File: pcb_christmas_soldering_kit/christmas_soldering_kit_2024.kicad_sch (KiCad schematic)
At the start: 23 parts, among them J3 Conn_Out, J4 Conn_In, J5 J_In, P1 Conn_01x08_Pin, P2 Conn_01x08_Pin, SW1 Button, U1 ESP32-C3, U2 TC4427CPA

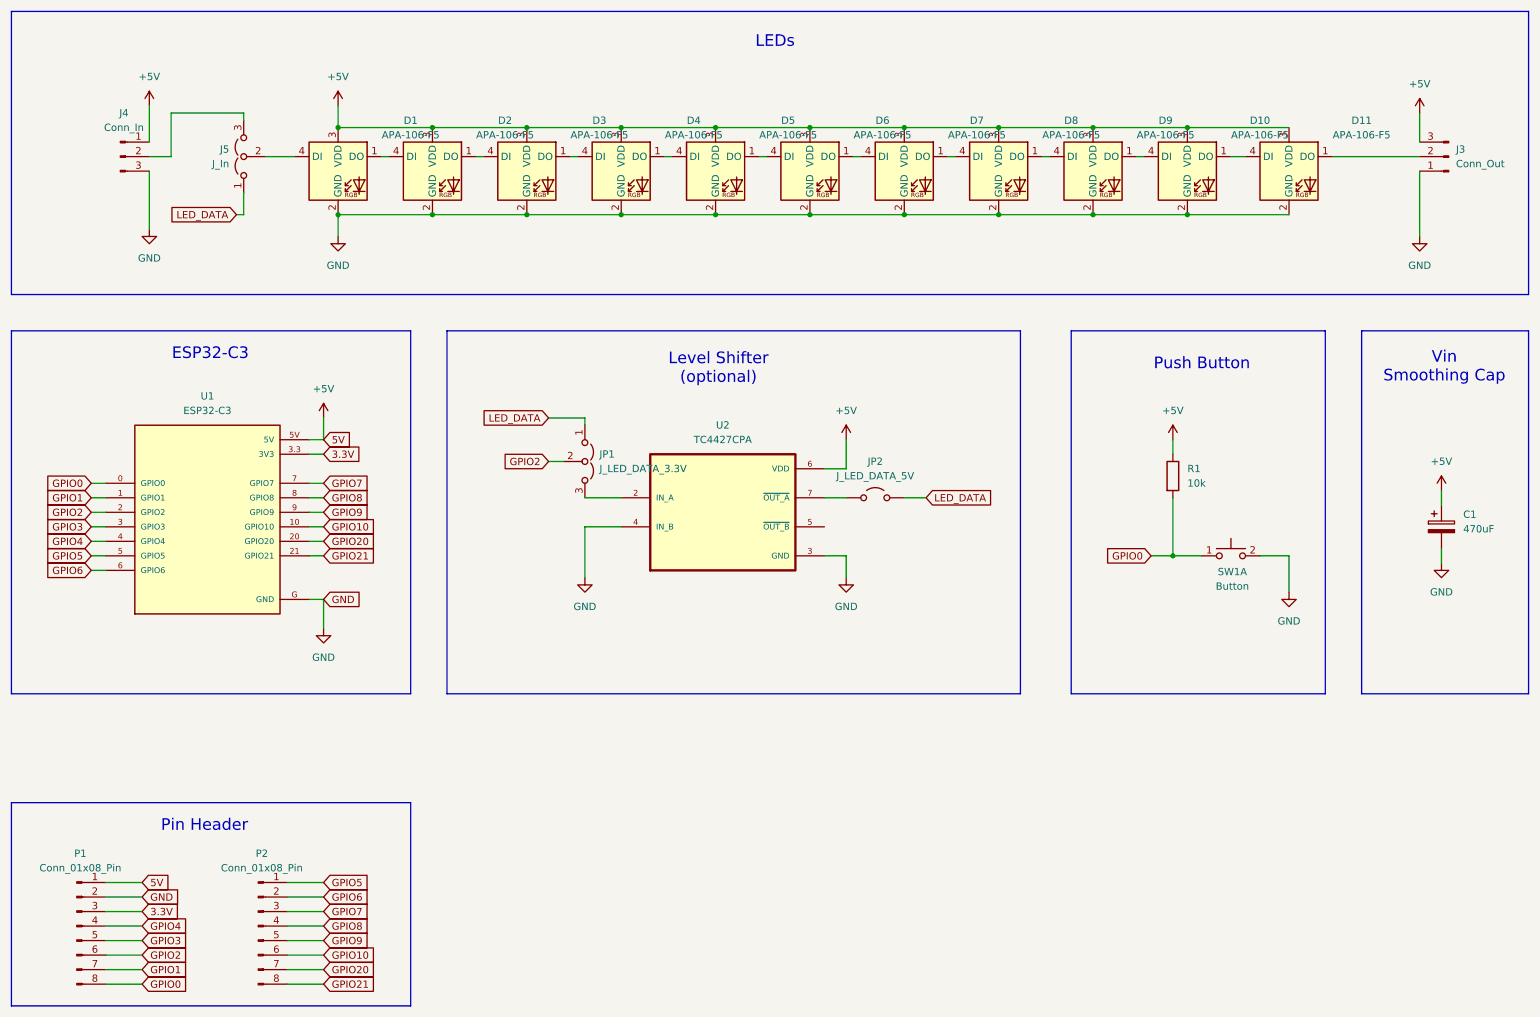
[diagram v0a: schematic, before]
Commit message: prototype 2: remove unnecessary components, improve LED footprints
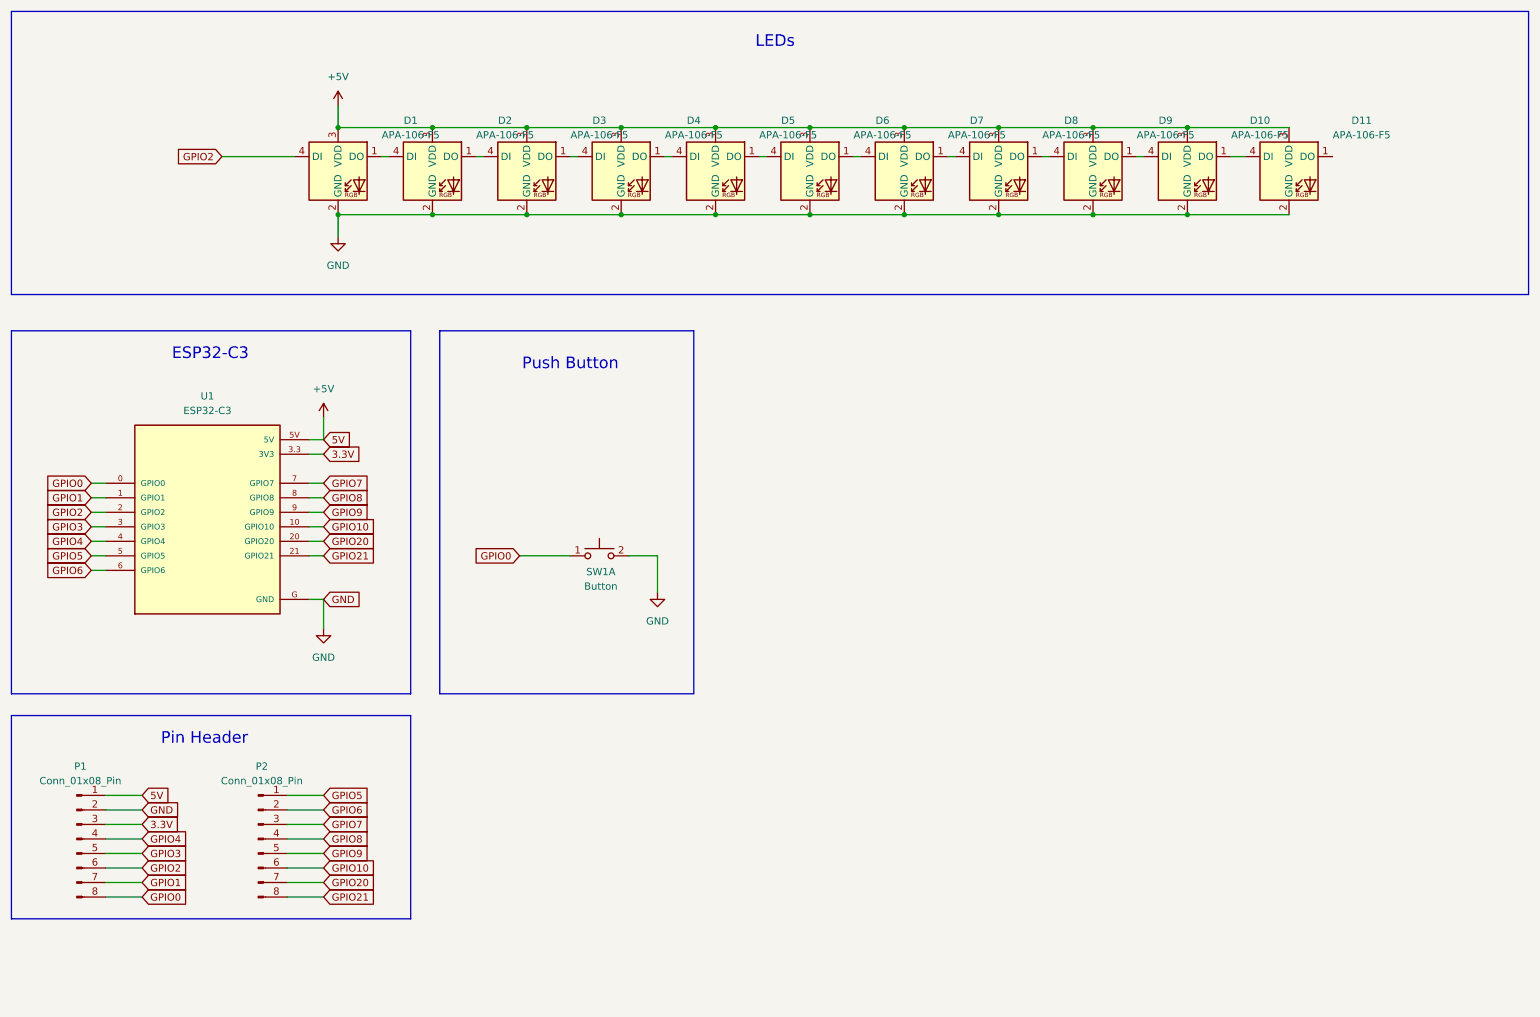
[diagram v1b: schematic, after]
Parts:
- removed C1: 470uF, Capacitor_THT:CP_Radial_D5.0mm_P2.50mm, symbol Device:C_Polarized
- removed J3: Conn_Out, Connector_JST:JST_XH_S3B-XH-A_1x03_P2.50mm_Horizontal, symbol Connector:Conn_01x03_Pin
- removed J4: Conn_In, Connector_JST:JST_XH_S3B-XH-A_1x03_P2.50mm_Horizontal, symbol Connector:Conn_01x03_Pin
- removed J5: J_In, Connector_PinHeader_2.54mm:PinHeader_1x03_P2.54mm_Vertical, symbol Jumper:Jumper_3_Open
- removed JP1: J_LED_DATA_3.3V, Jumper:SolderJumper-3_P1.3mm_Open_Pad1.0x1.5mm_NumberLabels, symbol Jumper:Jumper_3_Open
- removed JP2: J_LED_DATA_5V, Jumper:SolderJumper-2_P1.3mm_Open_TrianglePad1.0x1.5mm, symbol Jumper:Jumper_2_Open
- removed R1: 10k, Resistor_THT:R_Axial_DIN0207_L6.3mm_D2.5mm_P10.16mm_Horizontal, symbol Device:R
- removed U2: TC4427CPA, Package_DIP:DIP-8_W7.62mm, symbol TC4427CPA:TC4427CPA
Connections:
- net GPIO2: now also D1.4 (DI)
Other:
- note removed: "Level Shifter (optional)"
- note removed: "Vin Smoothing Cap"
- moved on the sheet: P1, P2, SW1A

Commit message: final version, rev. 1.0: ordered
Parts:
- added H1: MountingHole, MountingHole:MountingHole_2.2mm_M2, symbol Mechanical:MountingHole
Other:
- note added: "Mounting Hole"
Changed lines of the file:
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@@
+	)
+	(rectangle
+		(start 90.17 143.51)
+		(end 134.62 179.07)
+		(stroke
+			(width 0)
+			(type default)
+		)
+		(fill
+			(type none)
+		)
 	)
 	(rectangle
@@
 		)
 	)
+	(text "Mounting Hole"
+		(exclude_from_sim no)
+		(at 111.506 147.574 0)
+		(effects
+			(font
+				(size 2.032 2.032)
+			)
+		)
+	)
 	(text "LEDs"
 		(exclude_from_sim no)
@@
 			)
 		)
+	)
+	(symbol
+		(lib_id "Mechanical:MountingHole")
+		(at 106.68 161.29 0)
+		(unit 1)
+		(exclude_from_sim yes)
+		(in_bom no)
+		(on_board yes)
+		(dnp no)
+		(fields_autoplaced yes)
+		(property "Reference" "H1"
+			(at 109.22 160.0199 0)
+			(effects
+				(font
+					(size 1.27 1.27)
+				)
+				(justify left)
+			)
+		)
+		(property "Value" "MountingHole"
+			(at 109.22 162.5599 0)
+			(effects
+				(font
+					(size 1.27 1.27)
+				)
+				(justify left)
+			)
+		)
+		(property "Footprint" "MountingHole:MountingHole_2.2mm_M2"
+			(at 106.68 161.29 0)
+			(effects
+				(font
+					(size 1.27 1.27)
+				)
+				(hide yes)
+			)
+		)
+		(property "Datasheet" "~"
+			(at 106.68 161.29 0)
+			(effects
+				(font
+					(size 1.27 1.27)
+				)
+				(hide yes)
+			)
+		)
+		(property "Description" "Mounting Hole without connection"
+			(at 106.68 161.29 0)
+			(effects
+				(font
+					(size 1.27 1.27)
+				)
+				(hide yes)
+			)
+		)
+		(instances
+			(project ""
+				(path "/b5a58327-1640-4db5-89b9-8e71e13e26be"
+					(reference "H1")
+					(unit 1)
+				)
+			)
+		)
